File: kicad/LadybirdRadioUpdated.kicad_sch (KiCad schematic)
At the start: 42 parts, among them J1 VCap, J10 Conn_02x04_Odd_Even, J11 Conn_02x04_Odd_Even, J12 Conn_01x02_Pin, J2 Conn_01x02_Pin, J3 Conn_01x02_Pin, J4 Conn_01x03_Pin, J5 A/E, J8 Conn_02x04_Odd_Even, J9 Conn_01x02_Pin, Q1 BC547, Q2 BC337, Q3 BC337, T1 Transformer_P631T

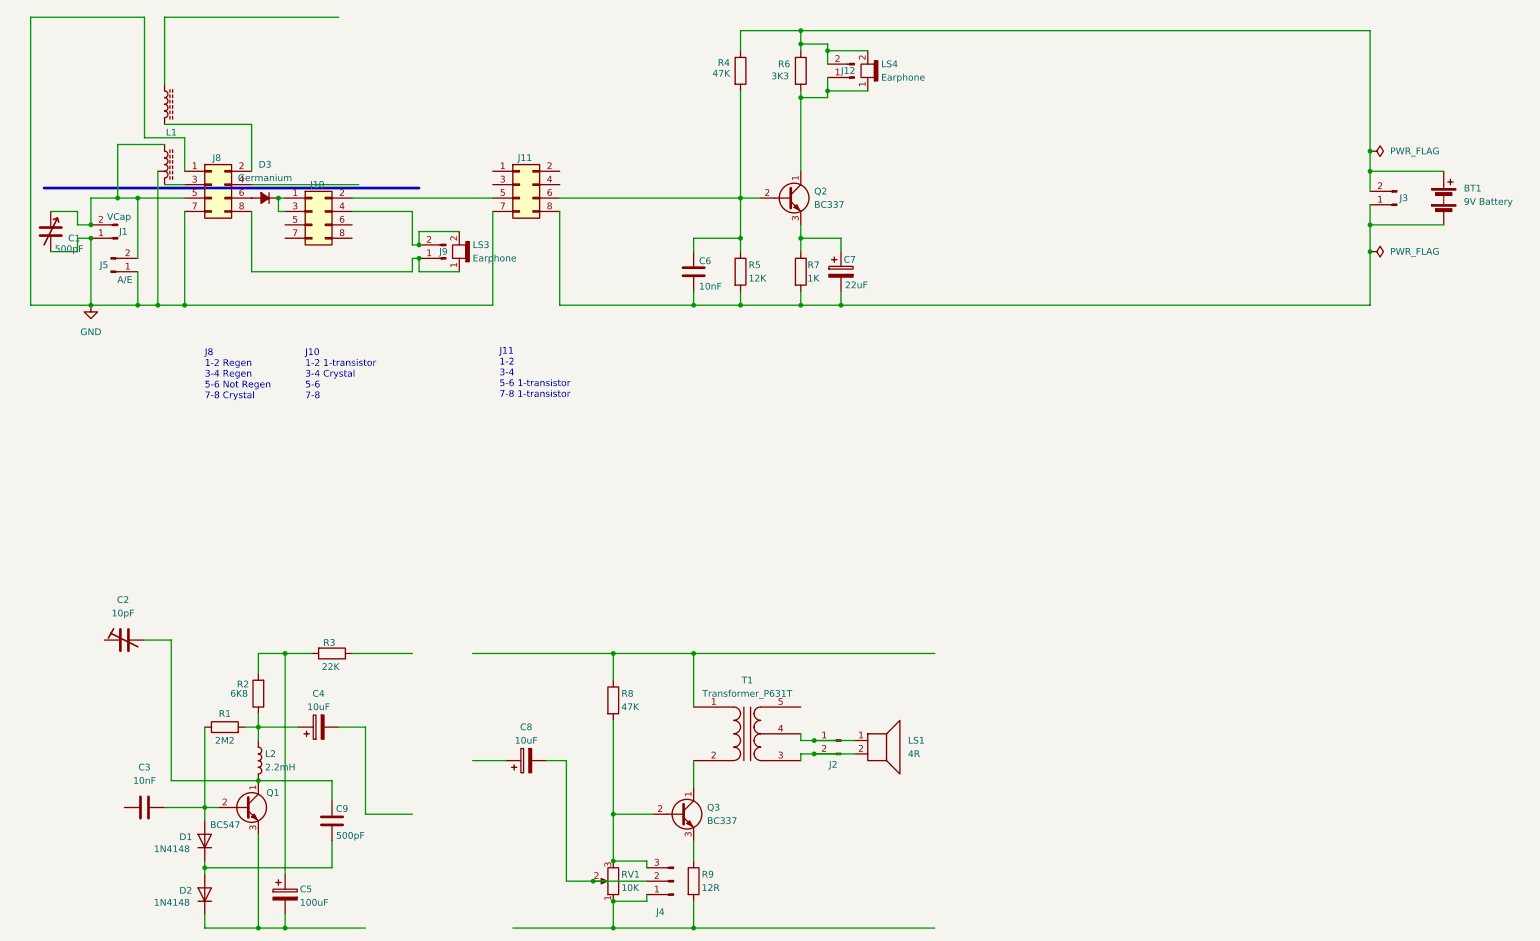
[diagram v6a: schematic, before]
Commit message: Added second transistor
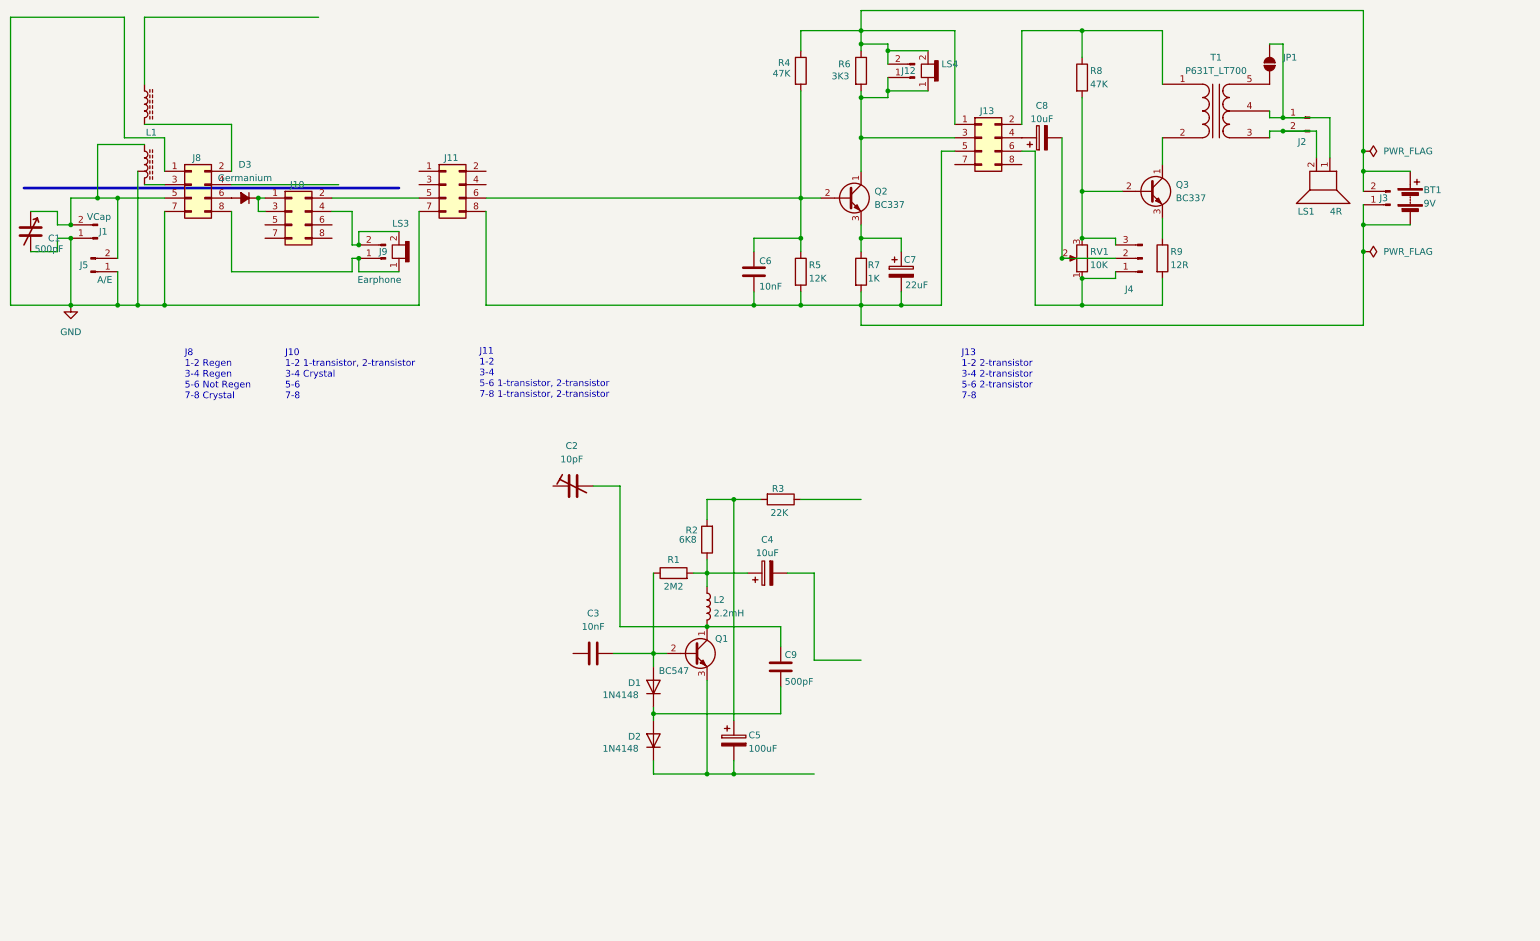
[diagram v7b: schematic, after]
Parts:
- added J13: Conn_02x04_Odd_Even, Connector_PinHeader_2.54mm:PinHeader_2x04_P2.54mm_Vertical, symbol Connector_Generic:Conn_02x04_Odd_Even
- added JP1: SolderJumper_2_Open, symbol Jumper:SolderJumper_2_Open
- BT1: value 9V Battery -> 9V
- T1: value Transformer_P631T -> P631T_LT700
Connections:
- net at R8.1, T1.1 (AA): now also J13.2 (Pin_2)
- net at J2.1 (Pin_1), LS1.1, T1.4 (SC): now also JP1.2 (B)
- net at T1.5 (SB): now also JP1.1 (A)
- net at BT1.2 (-), C6.2, C7.2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: now also J13.5 (Pin_5)
- net at J12.1 (Pin_1), LS4.1 (-), Q2.1 (C)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: now also J13.3 (Pin_3)
- net at BT1.1 (+), J12.2 (Pin_2), J3.2 (Pin_2)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: now also J13.1 (Pin_1)
- net at J4.1 (Pin_1), R9.2, RV1.1: now also J13.6 (Pin_6)
- net at C8.1: now also J13.4 (Pin_4)
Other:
- note added: "J10 1-2 1-transistor, 2-transistor 3-4 Crystal 5-6 7-8"
- note added: "J11 1-2 3-4 5-6 1-transistor, 2-transistor 7-8 1-transistor, 2-transistor"
- note added: "J13 1-2 2-transistor 3-4 2-transistor 5-6 2-transistor 7-8"
- note removed: "J10 1-2 1-transistor 3-4 Crystal 5-6 7-8"
- note removed: "J11 1-2 3-4 5-6 1-transistor 7-8 1-transistor"
- moved on the sheet: BT1, C1, C2, C3, C4, C5, C6, C7, C8, C9, D1, D2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

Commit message: Initial version with regen attached
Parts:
- removed J10, J11, J13, J8: Conn_02x04_Odd_Even, Connector_PinHeader_2.54mm:PinHeader_2x04_P2.54mm_Vertical, symbol Connector_Generic:Conn_02x04_Odd_Even
- added J10, J14, J6, J7: Conn_02x02_Odd_Even, Connector_PinHeader_2.54mm:PinHeader_2x02_P2.54mm_Vertical, symbol Connector_Generic:Conn_02x02_Odd_Even
- added J13, J8: Conn_02x03_Odd_Even, symbol Connector_Generic:Conn_02x03_Odd_Even
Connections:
- net GND: now also J9.1 (Pin_1), LS3.1 (-), J7.1 (Pin_1), J7.3 (Pin_3), J8.1 (Pin_1)
- net at C9.1, L2.2, Q1.1 (C): now also C2.1; no longer C2.2
- net at C1.1, J1.2 (Pin_2), J5.2 (Pin_2)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: now also J8.5 (Pin_5)
- net at R8.1, T1.1 (AA): now also J13.2 (Pin_2)
- net at C3.1: now also J8.4 (Pin_4)
- net at C6.1, Q2.2 (B), R4.2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: now also J14.2 (Pin_2), J14.4 (Pin_4)
- net at BT1.2 (-), C6.2, C7.2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: now also J13.5 (Pin_5), J7.2 (Pin_2)
- net at J12.1 (Pin_1), LS4.1 (-), Q2.1 (C)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: now also J13.3 (Pin_3)
- net at BT1.1 (+), J12.2 (Pin_2), J3.2 (Pin_2)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: now also J13.1 (Pin_1), J6.1 (Pin_1)
- net at C5.2, D2.1 (K), Q1.3 (E): now also J7.4 (Pin_4)
- net at J4.1 (Pin_1), R9.2, RV1.1: now also J13.6 (Pin_6)
- net at D3.1 (K): now also J10.1 (Pin_1), J10.3 (Pin_3)
- net at D3.2 (A): now also J8.6 (Pin_6)
- net at L1.4: now also J8.2 (Pin_2)
- net at L1.1: now also J8.3 (Pin_3)
- net at C8.1: now also J13.4 (Pin_4)
- net at J9.2 (Pin_2), LS3.2 (+): now also J10.4 (Pin_4)
- net at C4.2: now also J14.3 (Pin_3)
- net at L1.5: now also J6.3 (Pin_3)
- net at R3.1: now also J6.2 (Pin_2)
- new net: J10.2 (Pin_2), J14.1 (Pin_1)
- new net: C2.2, J6.4 (Pin_4)
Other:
- note added: "J10 1-2 1-transistor, 2-transistor 3-4 Crystal"
- note added: "J13 1-2 2-transistor, Regen 3-4 2-transistor, Regen 5-6 2-transistor, Regen"
- note added: "J14 1-2 1,2-transistor 3-4 Regen"
- note added: "J6 1-2 Regen 3-4 Regen J7 1-2 Not crystal 3-4 Regen"
- note added: "J8 1-2 Regen 3-4 Regen 5-6 Not Regen 7-8"
- note removed: "J10 1-2 1-transistor, 2-transistor 3-4 Crystal 5-6 7-8"
- note removed: "J11 1-2 3-4 5-6 1-transistor, 2-transistor 7-8 1-transistor, 2-transistor"
- note removed: "J13 1-2 2-transistor 3-4 2-transistor 5-6 2-transistor 7-8"
- note removed: "J8 1-2 Regen 3-4 Regen 5-6 Not Regen 7-8 Crystal"
- moved on the sheet: BT1, C2, C6, C7, C8, J12, J2, J3, J4, JP1, LS1, LS4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
